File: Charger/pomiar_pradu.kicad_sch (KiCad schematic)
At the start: 11 parts, among them Q17 IRF7404, Q18 IRF7404, Q19 BC846BW, U10 MCP6001-OT, U12 ACS712xLCTR-20A

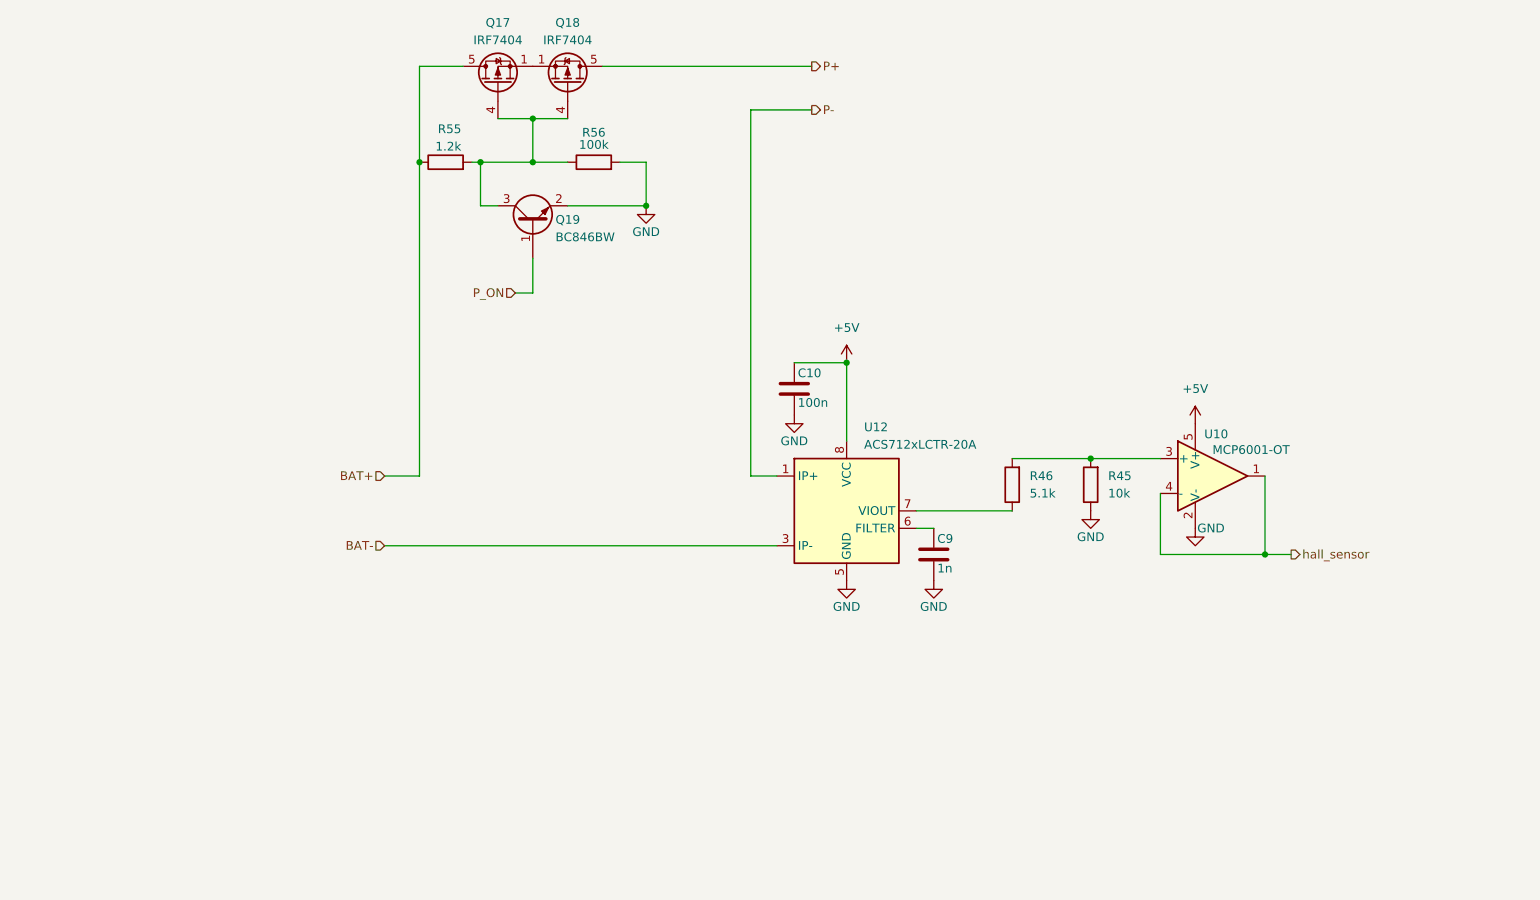
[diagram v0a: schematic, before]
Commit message: update
zakonczony schemat balansera, sztucznego obciazenia i pomiaru pradu. Przypisane wszystkie footprinty
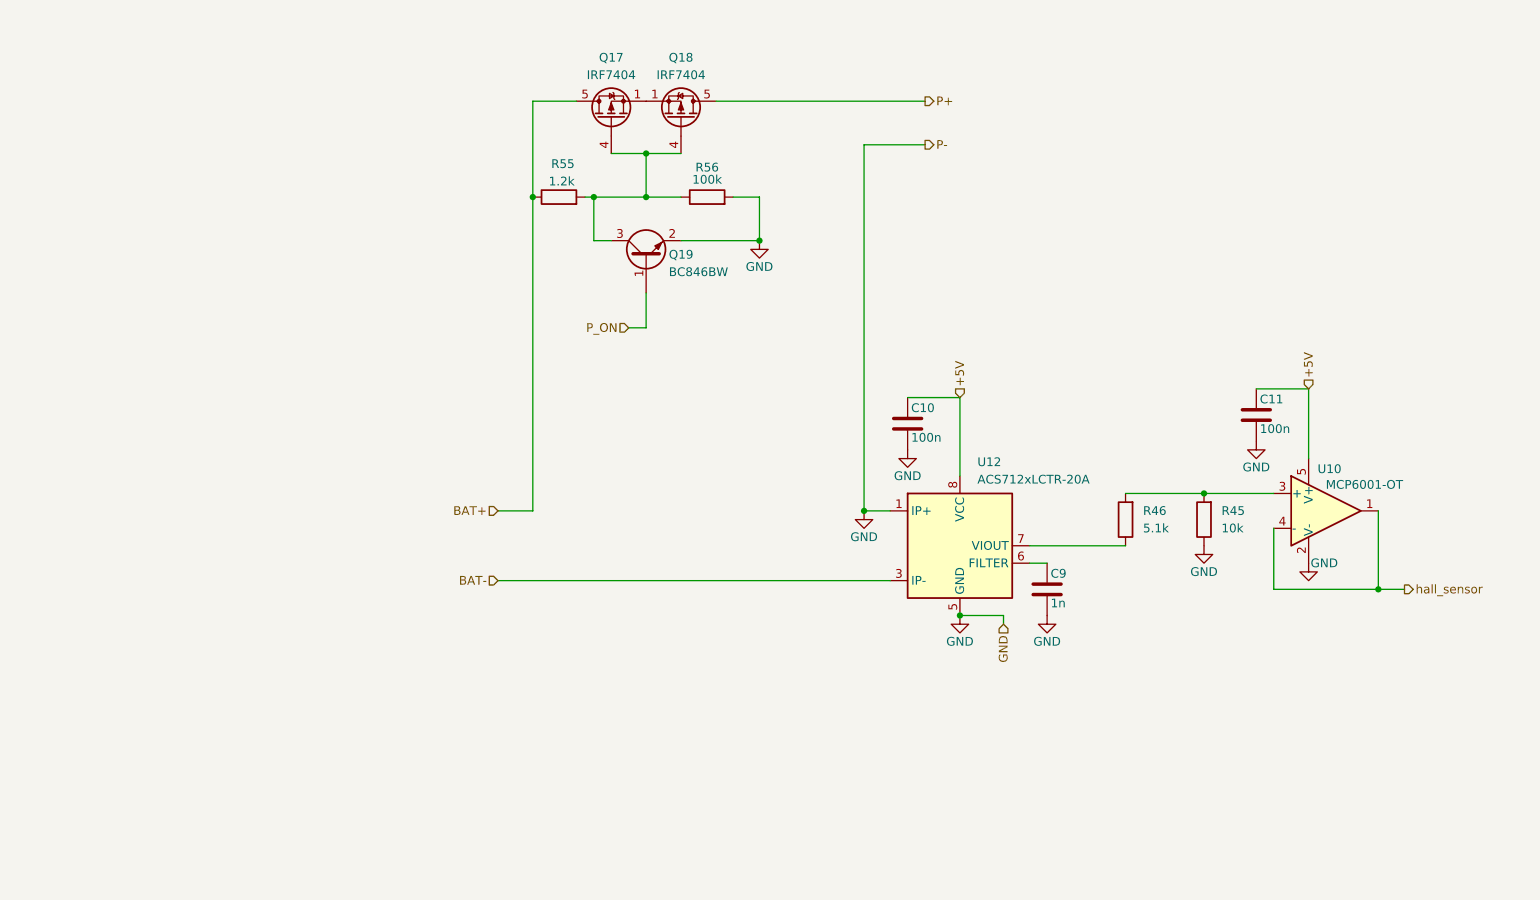
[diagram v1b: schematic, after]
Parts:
- added C11: 100n, Capacitor_SMD:C_0805_2012Metric_Pad1.18x1.45mm_HandSolder, symbol Device:C
- C9: footprint (none) -> Capacitor_SMD:C_0805_2012Metric_Pad1.18x1.45mm_HandSolder
- R45, R46: footprint (none) -> Resistor_SMD:R_0805_2012Metric_Pad1.20x1.40mm_HandSolder
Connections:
- net P- is gone; now on net GND: U12.1 (IP+), U12.2 (IP+)
- net +5V: now also C11.1
- net GND: now also C11.2
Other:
- moved on the sheet: C10, C9, Q17, Q18, Q19, R45, R46, R55, R56, U10, U12

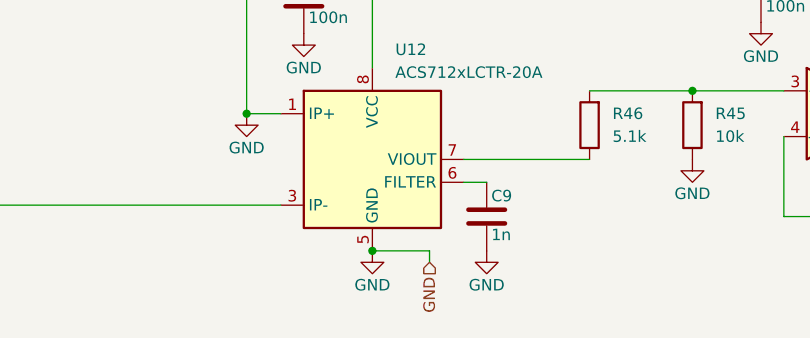
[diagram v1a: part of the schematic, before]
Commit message: dodana ladowarka do glownego projektu
drobne zmiany w sumie wszedzie pozbyłem sie 3.3v poza sterowaniem z pinów mcu, dopiescilem rezystorki zby bylo jak najmniej wartości rozszerzylem delikatnie zakres pradowy przetwornicy
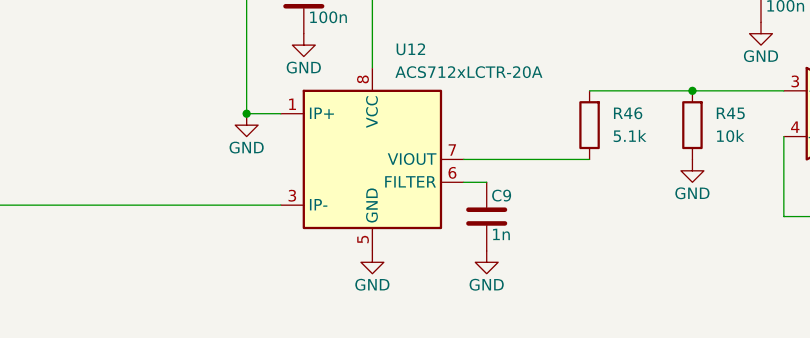
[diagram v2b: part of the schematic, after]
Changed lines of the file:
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@@
-	)
-	(junction
-		(at 149.86 130.81)
-		(diameter 0)
-		(color 0 0 0 0)
 	)
 	(junction
@@
 	(wire
 		(pts
-			(xy 156.21 130.81) (xy 156.21 132.08)
-		)
-		(stroke
-			(width 0)
-			(type default)
-		)
-	)
-	(wire
-		(pts
 			(xy 210.82 127) (xy 214.63 127)
 		)
@@
 	(wire
 		(pts
-			(xy 149.86 130.81) (xy 156.21 130.81)
-		)
-		(stroke
-			(width 0)
-			(type default)
-		)
-	)
-	(wire
-		(pts
 			(xy 160.02 120.65) (xy 173.99 120.65)
 		)
@@
 			(width 0)
 			(type default)
+		)
+	)
+	(hierarchical_label "P-"
+		(shape output)
+		(at 144.78 62.23 0)
+		(fields_autoplaced yes)
+		(effects
+			(font
+				(size 1.27 1.27)
+			)
+			(justify left)
+		)
+	)
+	(hierarchical_label "P+"
+		(shape output)
+		(at 144.78 55.88 0)
+		(fields_autoplaced yes)
+		(effects
+			(font
+				(size 1.27 1.27)
+			)
+			(justify left)
+		)
+	)
+	(hierarchical_label "BAT+"
+		(shape input)
+		(at 82.55 115.57 180)
+		(fields_autoplaced yes)
+		(effects
+			(font
+				(size 1.27 1.27)
+			)
+			(justify right)
+		)
+	)
+	(hierarchical_label "BAT-"
+		(shape input)
+		(at 82.55 125.73 180)
+		(fields_autoplaced yes)
+		(effects
+			(font
+				(size 1.27 1.27)
+			)
+			(justify right)
+		)
+	)
+	(hierarchical_label "P_ON"
+		(shape input)
+		(at 101.6 88.9 180)
+		(fields_autoplaced yes)
+		(effects
+			(font
+				(size 1.27 1.27)
+			)
+			(justify right)
+		)
+	)
+	(hierarchical_label "+5V"
+		(shape input)
+		(at 149.86 99.06 90)
+		(fields_autoplaced yes)
+		(effects
+			(font
+				(size 1.27 1.27)
+			)
+			(justify left)
 		)
 	)
@@
 		)
 	)
-	(hierarchical_label "P-"
-		(shape output)
-		(at 144.78 62.23 0)
-		(fields_autoplaced yes)
-		(effects
-			(font
-				(size 1.27 1.27)
-			)
-			(justify left)
-		)
-	)
-	(hierarchical_label "+5V"
-		(shape input)
-		(at 149.86 99.06 90)
-		(fields_autoplaced yes)
-		(effects
-			(font
-				(size 1.27 1.27)
-			)
-			(justify left)
-		)
-	)
-	(hierarchical_label "P+"
-		(shape output)
-		(at 144.78 55.88 0)
-		(fields_autoplaced yes)
-		(effects
-			(font
-				(size 1.27 1.27)
-			)
-			(justify left)
-		)
-	)
-	(hierarchical_label "BAT+"
-		(shape input)
-		(at 82.55 115.57 180)
-		(fields_autoplaced yes)
-		(effects
-			(font
-				(size 1.27 1.27)
-			)
-			(justify right)
-		)
-	)
-	(hierarchical_label "BAT-"
-		(shape input)
-		(at 82.55 125.73 180)
-		(fields_autoplaced yes)
-		(effects
-			(font
-				(size 1.27 1.27)
-			)
-			(justify right)
-		)
-	)
-	(hierarchical_label "GND"
-		(shape input)
-		(at 156.21 132.08 270)
-		(fields_autoplaced yes)
-		(effects
-			(font
-				(size 1.27 1.27)
-			)
-			(justify right)
-		)
-	)
-	(hierarchical_label "P_ON"
-		(shape input)
-		(at 101.6 88.9 180)
-		(fields_autoplaced yes)
-		(effects
-			(font
-				(size 1.27 1.27)
-			)
-			(justify right)
-		)
-	)

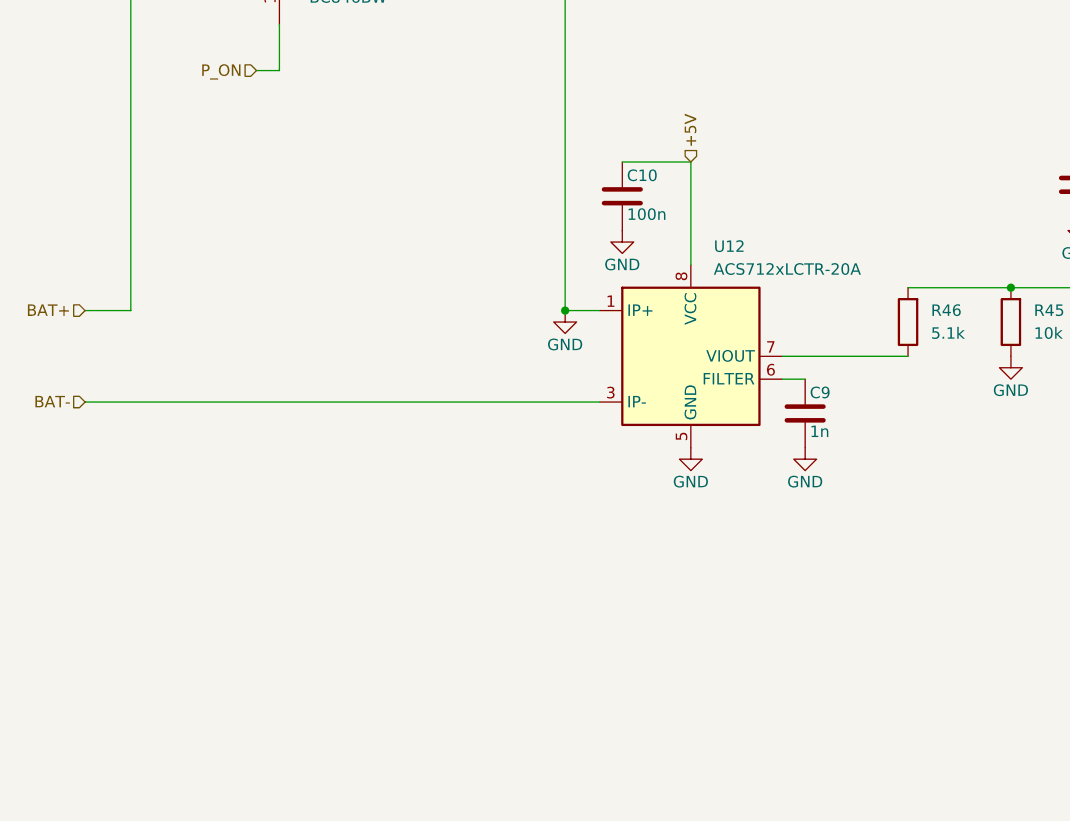
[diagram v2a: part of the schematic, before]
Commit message: dodany hall od tylu i opisy
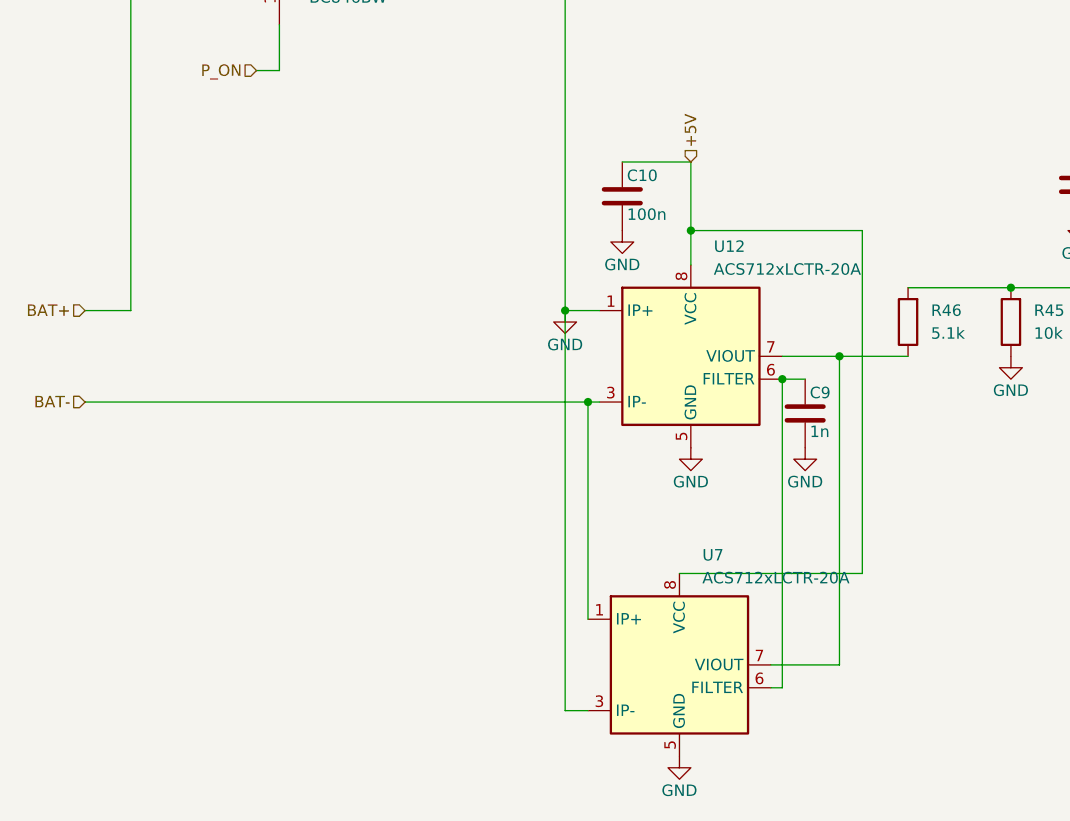
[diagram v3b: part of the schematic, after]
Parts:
- added U7: ACS712xLCTR-20A, Package_SO:SOIC-8_3.9x4.9mm_P1.27mm, symbol Sensor_Current:ACS712xLCTR-20A
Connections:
- net +5V: now also U7.8 (VCC)
- net BAT-: now also U7.1 (IP+), U7.2 (IP+)
- net GND: now also U7.3 (IP-), U7.4 (IP-), U7.5 (GND)
- net at R46.1, U12.7 (VIOUT): now also U7.7 (VIOUT)
- net at C9.1, U12.6 (FILTER): now also U7.6 (FILTER)

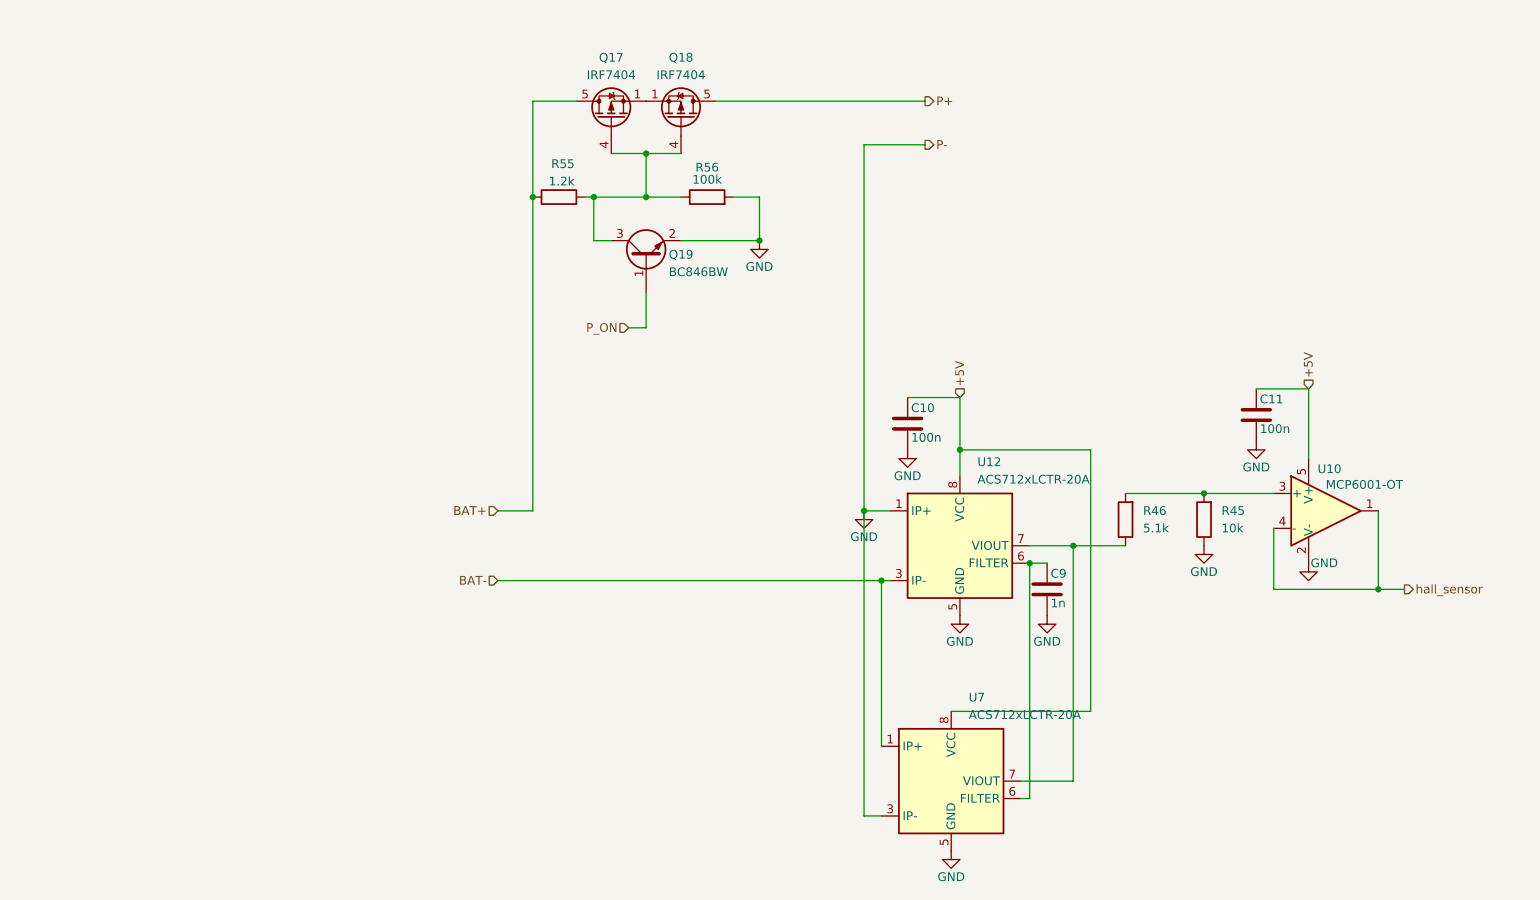
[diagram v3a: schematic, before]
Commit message: up
zmienione kilka sciezek, dodane przelotki do masy i rezystor do adc
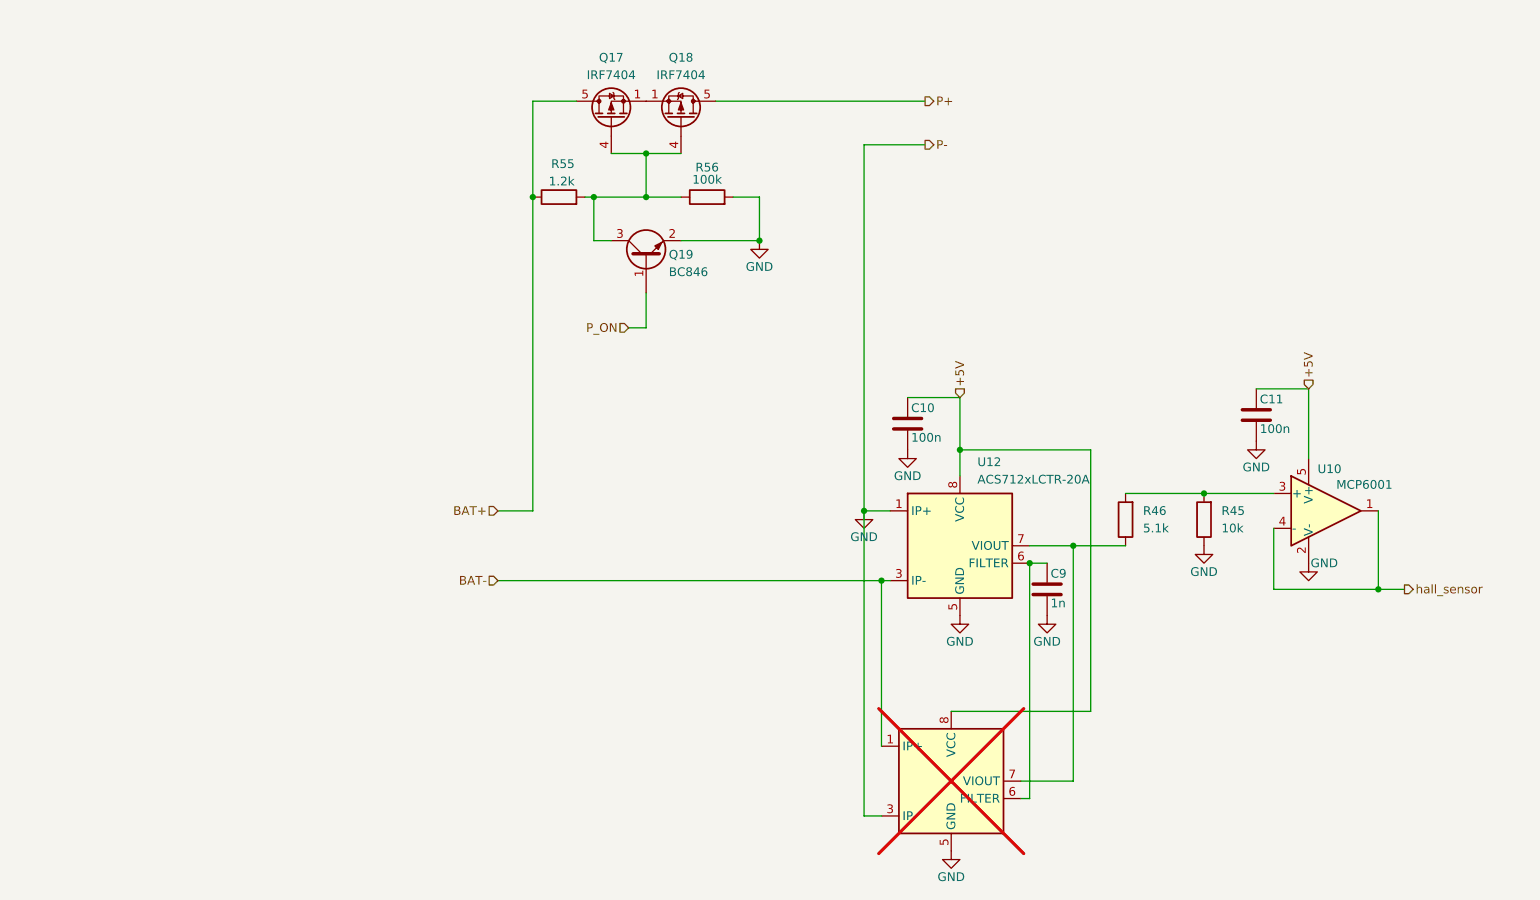
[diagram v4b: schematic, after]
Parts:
- Q19: value BC846BW -> BC846
- U10: value MCP6001-OT -> MCP6001
- U7: now not fitted; now left out of the parts list
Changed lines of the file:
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@@
 			)
 		)
-		(property "Value" "MCP6001-OT"
+		(property "Value" "MCP6001"
 			(at 208.788 111.76 0)
 			(effects
@@
 			)
 		)
-		(property "Value" "BC846BW"
+		(property "Value" "BC846"
 			(at 107.442 80.772 90)
 			(effects
@@
 		(unit 1)
 		(exclude_from_sim no)
-		(in_bom yes)
-		(on_board yes)
-		(dnp no)
+		(in_bom no)
+		(on_board yes)
+		(dnp yes)
 		(property "Reference" "U7"
 			(at 151.13 142.748 0)
@@
 				)
 				(justify left)
+				(hide yes)
 			)
 		)
@@
 				)
 				(justify left)
-			)
-		)
+				(hide yes)
+			)
+		)

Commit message: poprawki hardware
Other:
- note added: "r55 r56 to usuniecia w linie miedzy kolektorem Q19 a bramkami kosfetów dac rezystor 100k do glowniej lini zasilajacej"
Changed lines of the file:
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@@
+		)
+	)
+	(text "r55 r56 to usuniecia w linie miedzy kolektorem Q19 a bramkami kosfetów dac rezystor 100k do glowniej lini zasilajacej "
+		(exclude_from_sim no)
+		(at 83.82 96.52 0)
+		(effects
+			(font
+				(size 1.27 1.27)
+			)
 		)
 	)
